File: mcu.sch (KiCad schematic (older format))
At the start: 25 parts, among them IC1 ATMEGA168-A, P2 USB_B, SW1 SW_RESET, U4 FT232RL, U5 M25P16-VME, Y1 11.059MHz

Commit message: C24 was changed to an electrolytic capacitor
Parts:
- C24: footprint Capacitors_SMD:C_1206_HandSoldering -> SMD_Packages:SMD-1206_Pol; symbol C -> CP1_Small
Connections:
- net +3V3: now also C24.1; no longer C24.2
- net GND: now also C24.2; no longer C24.1
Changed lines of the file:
@@
 	9025 3800 9125 3800
 $Comp
-L C C24
+L CP1_Small C24
 U 1 1 584B750C
 P 7300 1925
 F 0 "C24" H 7325 2025 50  0000 L CNN
 F 1 "1uF" H 7325 1825 50  0000 L CNN
-F 2 "Capacitors_SMD:C_1206_HandSoldering" H 7338 1775 50  0001 C CNN
+F 2 "SMD_Packages:SMD-1206_Pol" H 7338 1775 50  0001 C CNN
 F 3 "" H 7300 1925 50  0000 C CNN
 	1    7300 1925
-	-1   0    0    1
+	1    0    0    -1
 $EndComp
 $Comp
@@
 $EndComp
 Wire Wire Line
-	7300 2075 7300 2125
-Wire Wire Line
-	7300 1775 7300 1750
-Wire Wire Line
 	7300 1750 6775 1750
 Connection ~ 6775 1750
+Wire Wire Line
+	7300 1750 7300 1825
+Wire Wire Line
+	7300 2025 7300 2125
 $EndSCHEMATC

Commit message: footprint of oscillator Y1 changed. Some silscreen changes
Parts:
- D2: symbol LED -> LED-RESCUE-lboard
- P2: symbol USB_B -> USB_B-RESCUE-lboard
- Y1: footprint Crystals:Crystal_HC52-U_Vertical -> Crystals:Crystal_HC49-U_Vertical
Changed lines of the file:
@@
 EESchema Schematic File Version 2
+LIBS:lboard-rescue
 LIBS:power
 LIBS:device
@@
 F 0 "Y1" H 4050 2275 50  0000 C CNN
 F 1 "11.059MHz" H 4050 1975 50  0000 C CNN
-F 2 "Crystals:Crystal_HC52-U_Vertical" H 4050 2125 50  0001 C CNN
+F 2 "Crystals:Crystal_HC49-U_Vertical" H 4050 2125 50  0001 C CNN
 F 3 "" H 4050 2125 50  0000 C CNN
 	1    4050 2125
@@
 $EndComp
 $Comp
-L LED D2
+L LED-RESCUE-lboard D2
 U 1 1 57E66175
 P 3575 725
+AR Path="/57E66175" Ref="D2"  Part="1"
+AR Path="/57DEC595/57E66175" Ref="D2"  Part="1"
 F 0 "D2" H 3575 825 50  0000 C CNN
 F 1 "LED" H 3575 625 50  0000 C CNN
@@
 $EndComp
 $Comp
-L USB_B P2
+L USB_B-RESCUE-lboard P2
 U 1 1 57E6ECB3
 P 1375 4950

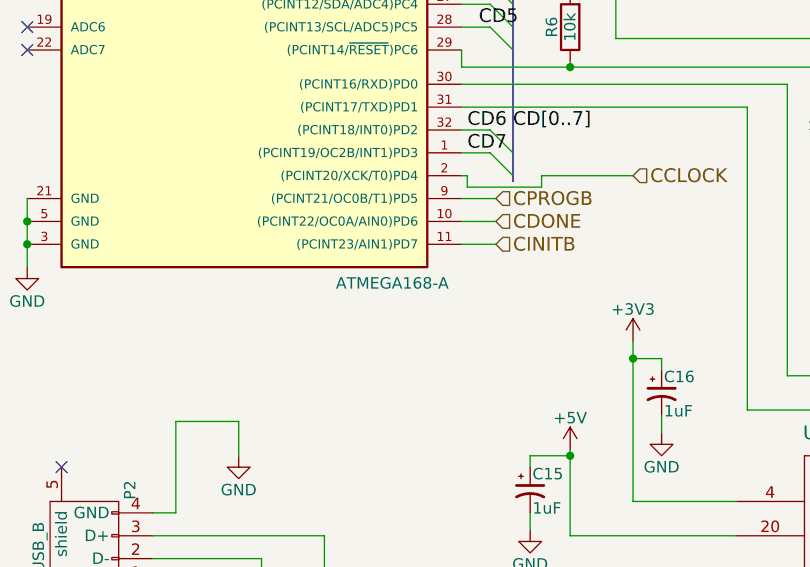
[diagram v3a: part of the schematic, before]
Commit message: ATMEGA168 description was changed to ATMEGA328P
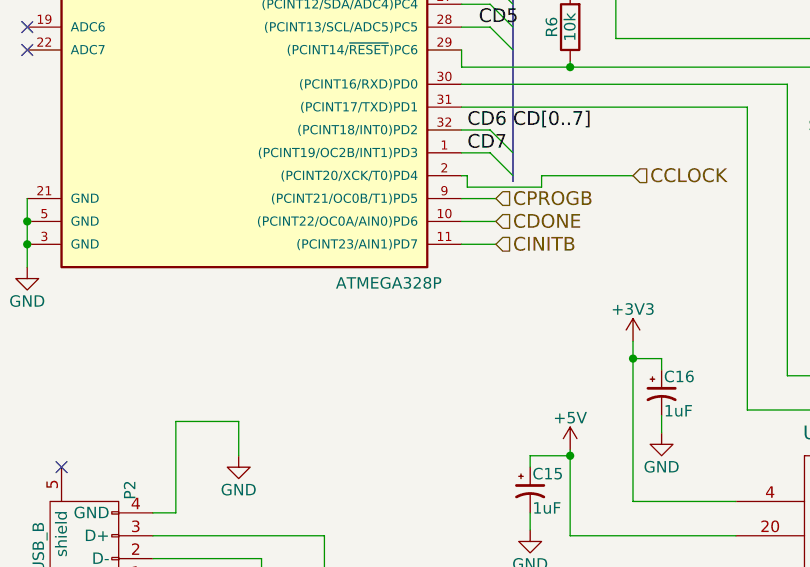
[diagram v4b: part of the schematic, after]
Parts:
- IC1: value ATMEGA168-A -> ATMEGA328P
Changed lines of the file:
@@
 P 2025 2475
 F 0 "IC1" H 1275 3725 50  0000 L BNN
-F 1 "ATMEGA168-A" H 2475 1075 50  0000 L BNN
+F 1 "ATMEGA328P" H 2475 1075 50  0000 L BNN
 F 2 "Housings_QFP:TQFP-32_7x7mm_Pitch0.8mm" H 2025 2475 50  0001 C CIN
 F 3 "" H 2025 2475 50  0000 C CNN
